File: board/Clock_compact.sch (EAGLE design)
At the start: 18 parts

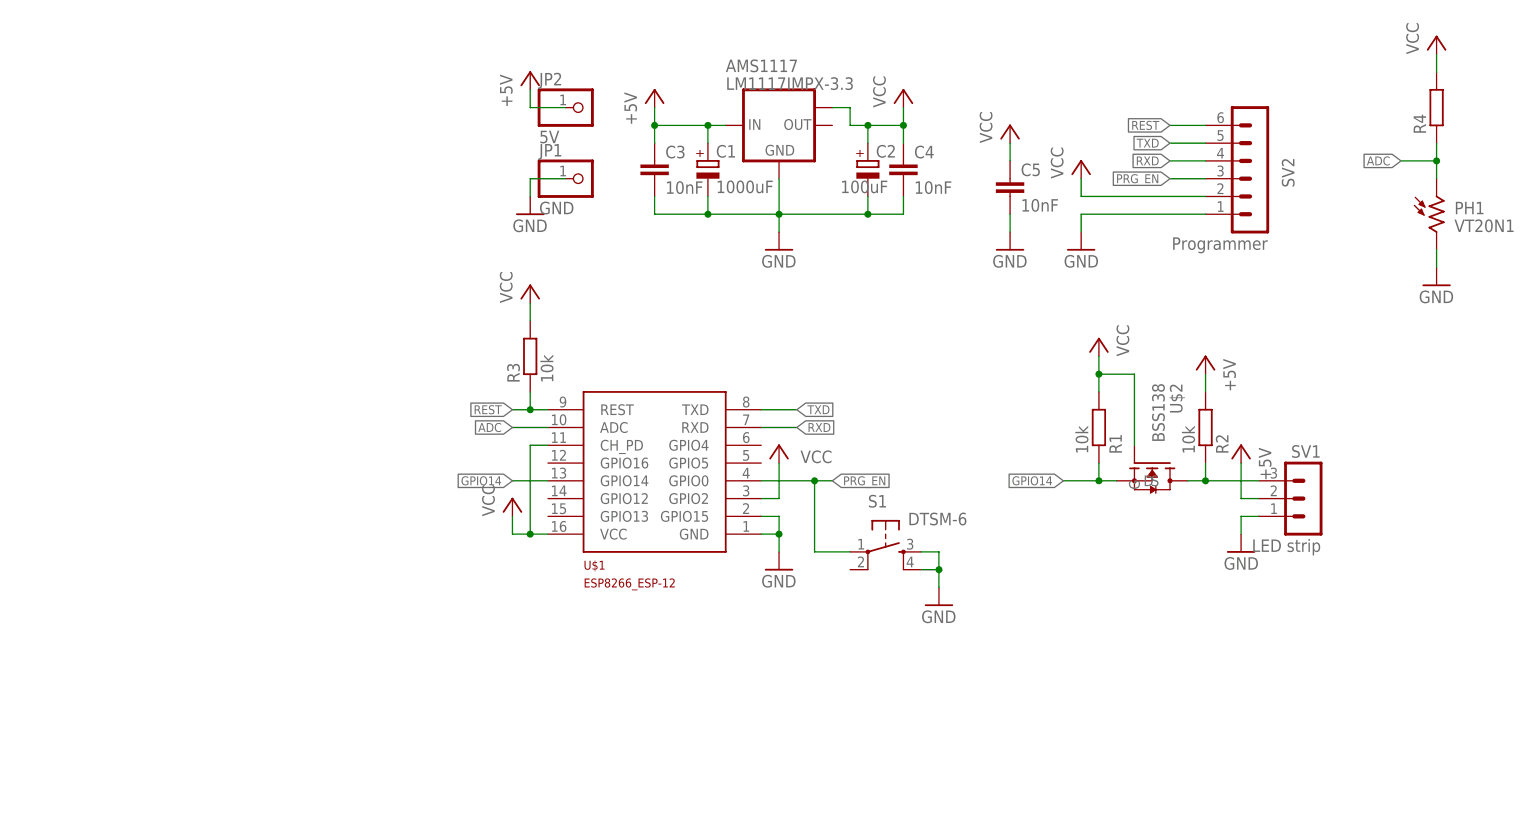
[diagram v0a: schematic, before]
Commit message: Removed LEDs, organised PCB files
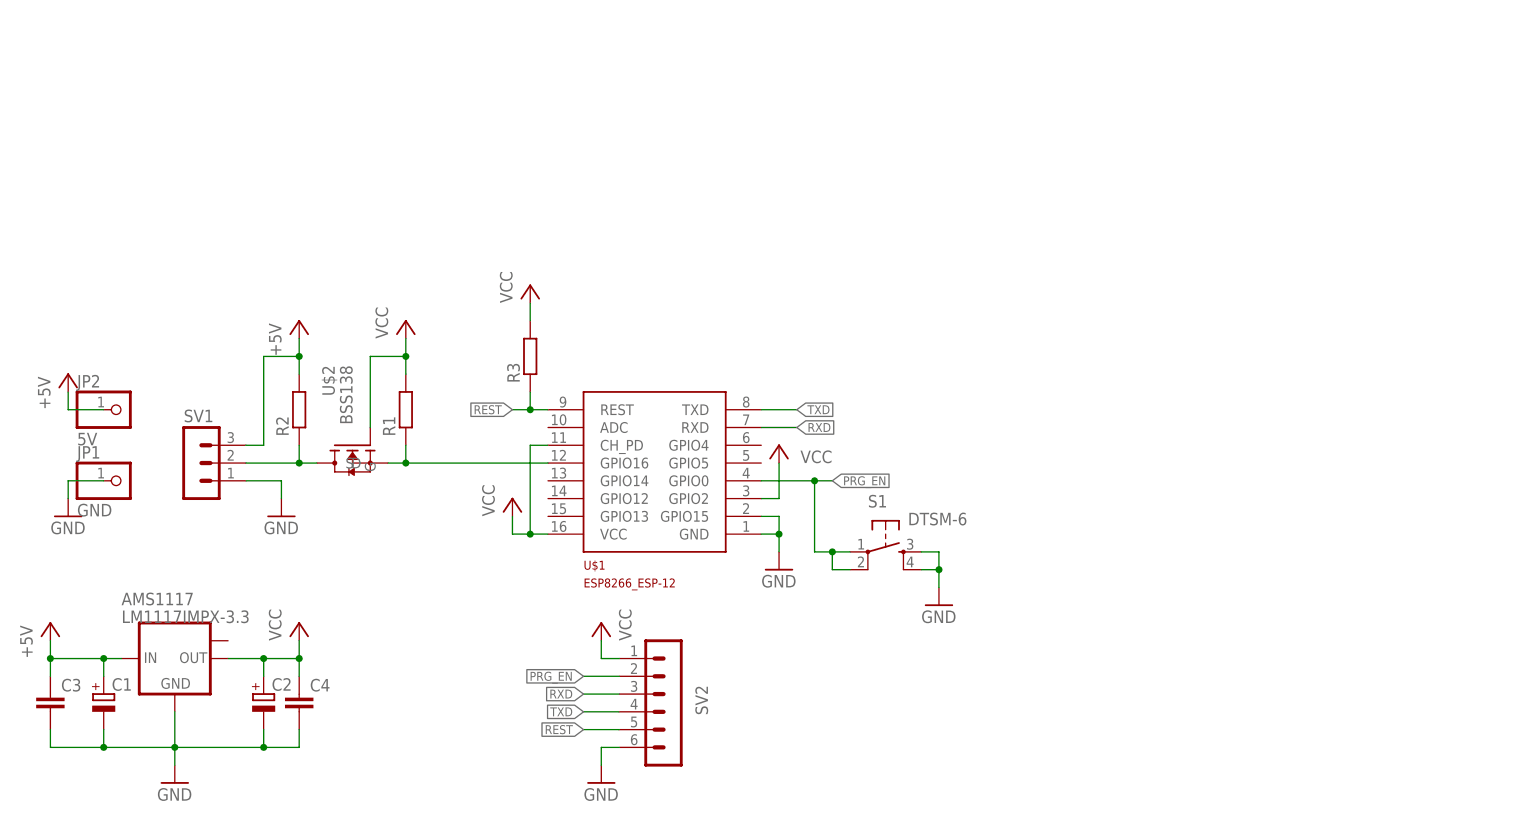
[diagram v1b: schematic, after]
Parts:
- removed C5: 10nF, rcl:C-EUC0805
- removed PH1: VT20N1, photo-elements:VT20N1
- removed R4: (no value), rcl:R-EU_R0805
- C1: value 1000uF -> (none); device rcl:CPOL-EUTT5D11L -> rcl:CPOL-EUE3.5-8
- C2: value 100uF -> (none); device rcl:CPOL-EUTT5D7L -> rcl:CPOL-EUE3.5-8
- C3, C4: value 10nF -> (none)
- R1, R2, R3: value 10k -> (none)
- SV1: value LED strip -> (none)
- SV2: value Programmer -> (none)
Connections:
- removed net ADC: PH1.1, R4.1, U$1.ADC
- removed net GPIO14: R1.1, U$1.GPIO14, U$2.S
- new net N$9: R1.1, U$1.GPIO16, U$2.S
- net +5V: now also SV1.3; no longer SV1.2
- net GND: now also SV2.6; no longer C5.2, PH1.2, SV2.1
- net N$7: now also SV1.2; no longer SV1.3
- net PRG_EN: now also S1.2, SV2.2; no longer SV2.3
- net REST: now also SV2.5; no longer SV2.6
- net RXD: now also SV2.3; no longer SV2.4
- net TXD: now also SV2.4; no longer SV2.5
- net VCC: now also AMS1117.OUT, SV2.1; no longer AMS1117.OUT1, C5.1, R4.2, SV2.2
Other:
- moved on the sheet: AMS1117, C1, C2, C3, C4, JP1, JP2, R1, R2, SV1, SV2, U$2
